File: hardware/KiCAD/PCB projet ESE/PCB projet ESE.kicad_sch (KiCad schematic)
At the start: 49 parts, among them J1 Conn_01x06, J2 Conn_01x04, J3 Conn_01x06, J4 Conn_01x06, J5 Conn_01x02, J6 Conn_01x04, J7 Conn_ST_STDC14, SW1 SW_SPST, SW2 472121010111, U1 ZXBM5210-SP, U2 ZXBM5210-SP, U3 STM32G474RETx, U4 ADXL343

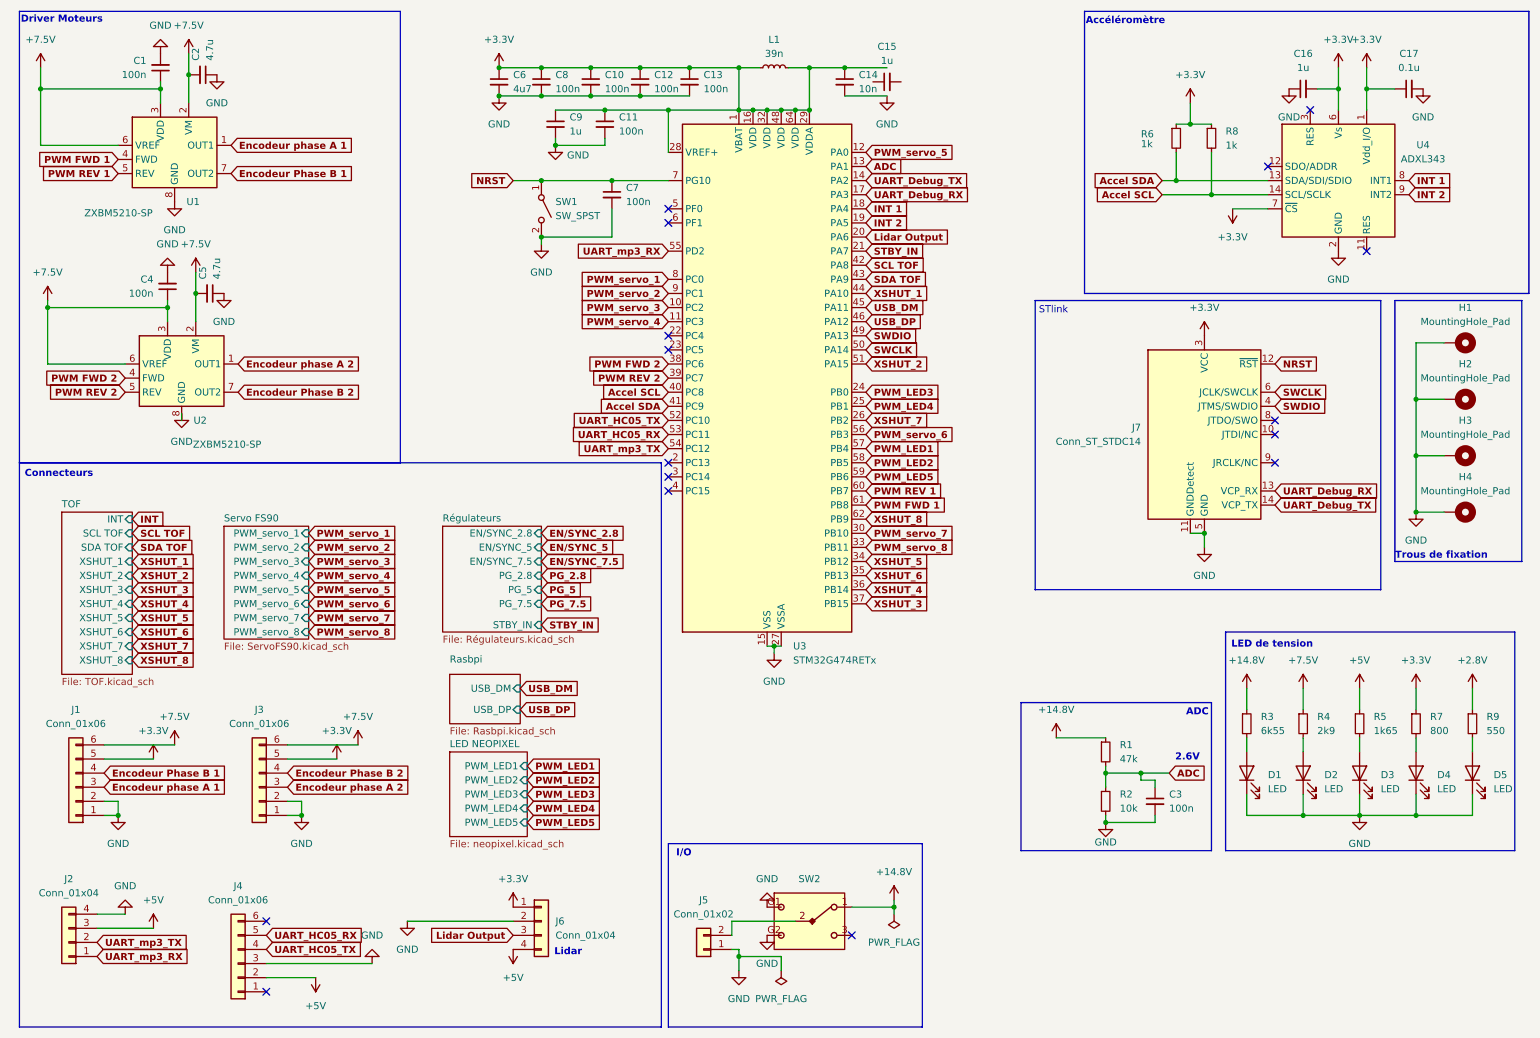
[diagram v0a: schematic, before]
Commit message: maj schematic & pinout CubeIDE
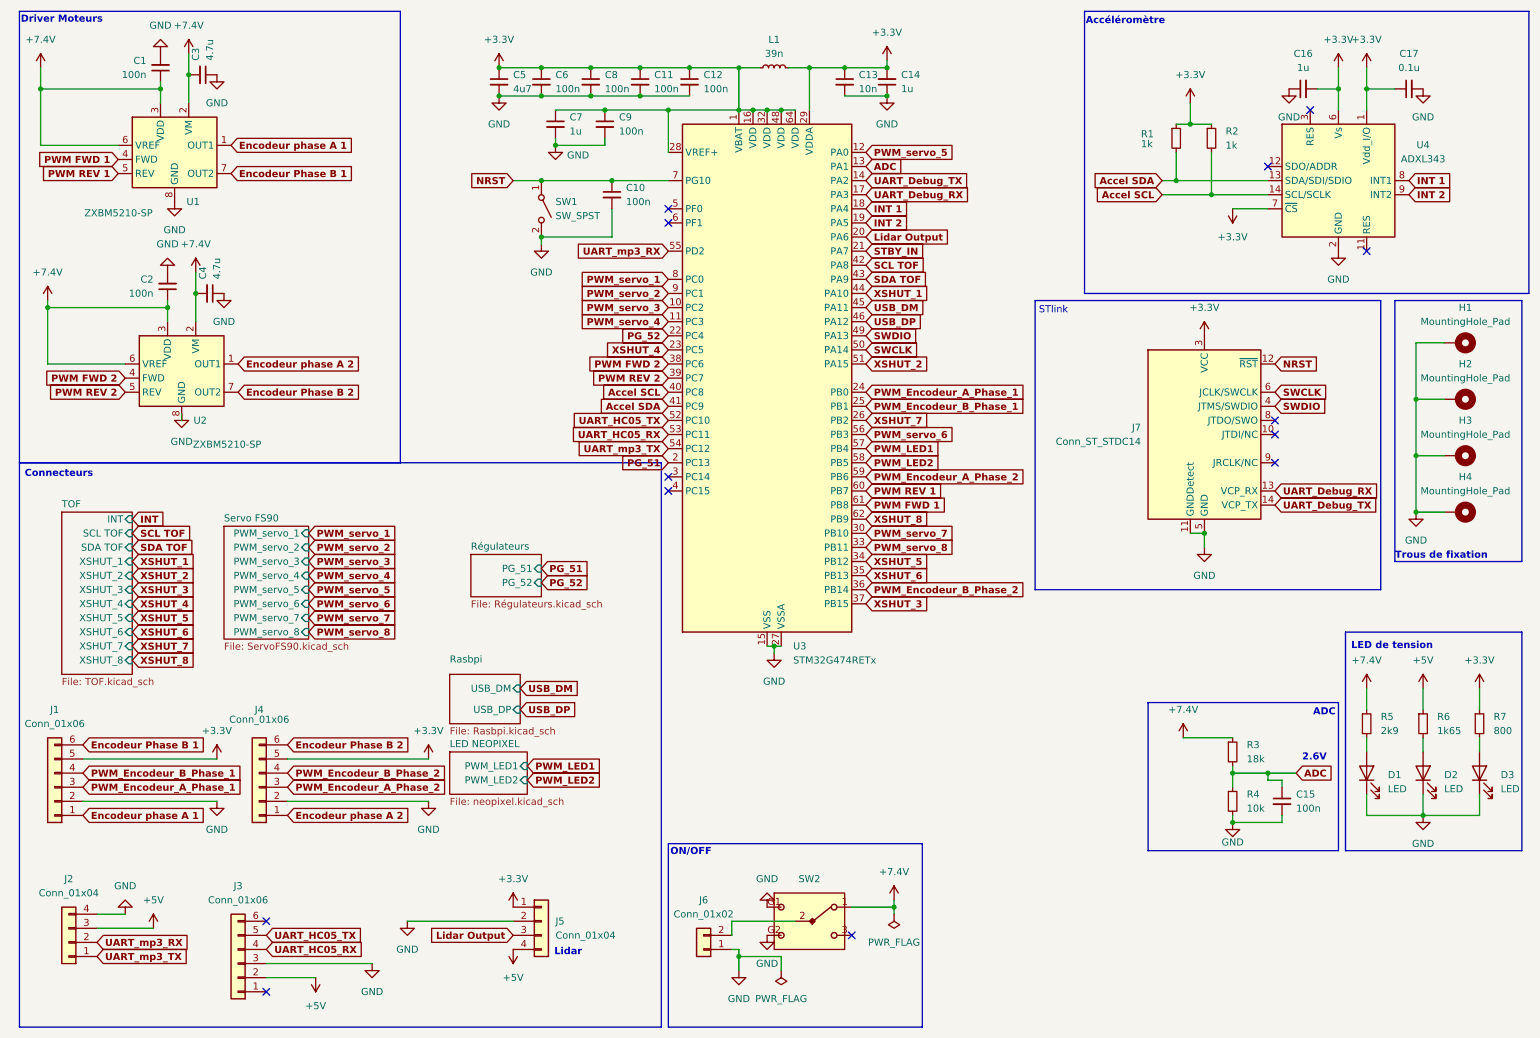
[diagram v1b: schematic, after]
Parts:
- removed D1, D5: LED, LED_SMD:LED_0603_1608Metric, symbol Device:LED
- removed R3: 6k55, Resistor_SMD:R_0402_1005Metric, symbol Device:R_Small
- removed R9: 550, Resistor_SMD:R_0402_1005Metric, symbol Device:R_Small
- J6: renamed from J5; footprint Connector_AMASS:AMASS_XT60-M_1x02_P7.20mm_Vertical -> Connector_AMASS:AMASS_XT30U-M_1x02_P5.0mm_Vertical
- R3: renamed from R1; value 47k -> 18k
- renumbered C7 to C10, C12 to C11, C13 to C12, C14 to C13, C15 to C14, C3 to C15, C4 to C2, C2 to C3, C5 to C4, C6 to C5, C8 to C6, C9 to C7, C10 to C8, C11 to C9, D2 to D1, D3 to D2, D4 to D3, J4 to J3, J3 to J4, J6 to J5, R6 to R1, R8 to R2, R2 to R4, R4 to R5, R5 to R6
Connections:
- net +3.3V: now also C14.2
- net Encodeur Phase B 1: now also J1.6 (Pin_6); no longer J1.4 (Pin_4)
- net Encodeur Phase B 2: now also J4.6 (Pin_6); no longer J4.4 (Pin_4)
- net Encodeur phase A 1: now also J1.1 (Pin_1); no longer J1.3 (Pin_3)
- net Encodeur phase A 2: now also J4.1 (Pin_1); no longer J4.3 (Pin_3)
- net GND: now also C14.1; no longer J1.1 (Pin_1), J4.1 (Pin_1)
- net UART_HC05_RX: now also J3.4 (Pin_4); no longer J3.5 (Pin_5)
- net UART_HC05_TX: now also J3.5 (Pin_5); no longer J3.4 (Pin_4)
- net UART_mp3_RX: now also J2.2 (Pin_2); no longer J2.1 (Pin_1)
- net UART_mp3_TX: now also J2.1 (Pin_1); no longer J2.2 (Pin_2)
- net XSHUT_4: now also U3.23 (PC5); no longer U3.36 (PB14)
- net PG_51: now reaches U3.2 (PC13)
- net PG_52: now reaches U3.22 (PC4)
- net +14.8V renamed +7.4V
- net +7.4V: now also C1.1, C2.1, C3.2, C4.2, R5.1, U1.2 (VM), U1.3 (VDD), U1.6 (VREF), U2.2 (VM), U2.3 (VDD), U2.6 (VREF)
- removed net +7.5V: C1.1, C2.1, C3.2, C4.2, J1.6 (Pin_6), J4.6 (Pin_6), R5.1, U1.2 (VM), U1.3 (VDD), U1.6 (VREF), U2.2 (VM), U2.3 (VDD), U2.6 (VREF)
- net PWM_LED3 renamed PWM_Encodeur_A_Phase_1
- net PWM_Encodeur_A_Phase_1: now also J1.3 (Pin_3)
- net PWM_LED4 renamed PWM_Encodeur_B_Phase_1
- net PWM_Encodeur_B_Phase_1: now also J1.4 (Pin_4)
- net PWM_LED5 renamed PWM_Encodeur_A_Phase_2
- net PWM_Encodeur_A_Phase_2: now also J4.3 (Pin_3)
- new net PWM_Encodeur_B_Phase_2: J4.4 (Pin_4), U3.36 (PB14)
- no-connect marks 16 -> 13
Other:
- sheet LED NEOPIXEL ports: added none; removed PWM_LED3, PWM_LED4, PWM_LED5
- sheet Régulateurs ports: added PG_51, PG_52; removed EN/SYNC_2.8, EN/SYNC_5, EN/SYNC_7.5, PG_2.8, PG_5, PG_7.5, STBY_IN
- note added: "ON/OFF"
- note removed: "I/O"
- moved on the sheet: C14, C15, D1, D2, D3, J1, R3, R4, R5, R6, R7

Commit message: maj schematic
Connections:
- net ADC renamed ADC1_IN2
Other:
- moved on the sheet: C15, R3, R4
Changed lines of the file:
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@@
 	)
 	(rectangle
-		(start 215.9 137.16)
+		(start 210.82 137.16)
 		(end 250.19 163.83)
 		(stroke
@@
 	(text "ADC"
 		(exclude_from_sim no)
-		(at 247.65 138.938 0)
+		(at 242.57 138.938 0)
 		(effects
 			(font
@@
 	(text "2.6V"
 		(exclude_from_sim no)
-		(at 245.872 147.066 0)
+		(at 240.792 147.066 0)
 		(effects
 			(font
@@
 	)
 	(junction
-		(at 231.14 149.86)
+		(at 226.06 149.86)
 		(diameter 0)
 		(color 0 0 0 0)
@@
 	)
 	(junction
-		(at 237.49 149.86)
+		(at 232.41 149.86)
 		(diameter 0)
 		(color 0 0 0 0)
@@
 	)
 	(junction
-		(at 231.14 158.75)
+		(at 226.06 158.75)
 		(diameter 0)
 		(color 0 0 0 0)
@@
 	(wire
 		(pts
-			(xy 231.14 149.86) (xy 231.14 152.4)
+			(xy 226.06 149.86) (xy 226.06 152.4)
 		)
 		(stroke
@@
 	(wire
 		(pts
-			(xy 231.14 148.59) (xy 231.14 149.86)
+			(xy 226.06 148.59) (xy 226.06 149.86)
 		)
 		(stroke
@@
 	(wire
 		(pts
-			(xy 240.03 157.48) (xy 240.03 158.75)
+			(xy 234.95 157.48) (xy 234.95 158.75)
 		)
 		(stroke
@@
 	(wire
 		(pts
-			(xy 231.14 158.75) (xy 231.14 157.48)
+			(xy 226.06 158.75) (xy 226.06 157.48)
 		)
 		(stroke
@@
 	(wire
 		(pts
-			(xy 240.03 158.75) (xy 231.14 158.75)
+			(xy 234.95 158.75) (xy 226.06 158.75)
 		)
 		(stroke
@@
 	(wire
 		(pts
-			(xy 240.03 152.4) (xy 240.03 151.13)
+			(xy 234.95 152.4) (xy 234.95 151.13)
 		)
 		(stroke
@@
 	(wire
 		(pts
-			(xy 237.49 149.86) (xy 231.14 149.86)
+			(xy 232.41 149.86) (xy 226.06 149.86)
 		)
 		(stroke
@@
 	(wire
 		(pts
-			(xy 242.57 149.86) (xy 237.49 149.86)
+			(xy 237.49 149.86) (xy 232.41 149.86)
 		)
 		(stroke
@@
 	(wire
 		(pts
-			(xy 222.25 143.51) (xy 231.14 143.51)
+			(xy 217.17 143.51) (xy 226.06 143.51)
 		)
 		(stroke
@@
 	(wire
 		(pts
-			(xy 237.49 151.13) (xy 237.49 149.86)
+			(xy 232.41 151.13) (xy 232.41 149.86)
 		)
 		(stroke
@@
 	(wire
 		(pts
-			(xy 240.03 151.13) (xy 237.49 151.13)
+			(xy 234.95 151.13) (xy 232.41 151.13)
 		)
 		(stroke
@@
 		)
 	)
-	(global_label "ADC"
+	(global_label "ADC1_IN2"
 		(shape input)
-		(at 242.57 149.86 0)
+		(at 237.49 149.86 0)
 		(fields_autoplaced yes)
 		(effects
@@
 		)
 		(property "Intersheetrefs" "${INTERSHEET_REFS}"
-			(at 249.6598 149.86 0)
+			(at 249.9017 149.86 0)
 			(effects
 				(font
@@
 		)
 	)
-	(global_label "ADC"
+	(global_label "ADC1_IN2"
 		(shape input)
 		(at 165.1 40.64 0)
@@
 		)
 		(property "Intersheetrefs" "${INTERSHEET_REFS}"
-			(at 172.1898 40.64 0)
+			(at 177.5117 40.64 0)
 			(effects
 				(font
@@
 	(symbol
 		(lib_id "Device:R_Small")
-		(at 231.14 154.94 0)
+		(at 226.06 154.94 0)
 		(unit 1)
 		(exclude_from_sim no)
@@
 		(fields_autoplaced yes)
 		(property "Reference" "R4"
-			(at 233.68 153.6699 0)
+			(at 228.6 153.6699 0)
 			(effects
 				(font
@@
 		)
 		(property "Value" "10k"
-			(at 233.68 156.2099 0)
+			(at 228.6 156.2099 0)
 			(effects
 				(font
@@
 		)
 		(property "Footprint" "Resistor_SMD:R_0402_1005Metric"
-			(at 231.14 154.94 0)
+			(at 226.06 154.94 0)
 			(effects
 				(font
@@
 		)
 		(property "Datasheet" "~"
-			(at 231.14 154.94 0)
+			(at 226.06 154.94 0)
 			(effects
 				(font
@@
 		)
 		(property "Description" "Resistor, small symbol"
-			(at 231.14 154.94 0)
+			(at 226.06 154.94 0)
 			(effects
 				(font
@@
 	(symbol
 		(lib_id "Device:R_Small")
-		(at 231.14 146.05 0)
+		(at 226.06 146.05 0)
 		(unit 1)
 		(exclude_from_sim no)
@@
 		(fields_autoplaced yes)
 		(property "Reference" "R3"
-			(at 233.68 144.7799 0)
+			(at 228.6 144.7799 0)
 			(effects
 				(font
@@
 		)
 		(property "Value" "18k"
-			(at 233.68 147.3199 0)
+			(at 228.6 147.3199 0)
 			(effects
 				(font
@@
 		)
 		(property "Footprint" "Resistor_SMD:R_0402_1005Metric"
-			(at 231.14 146.05 0)
+			(at 226.06 146.05 0)
 			(effects
 				(font
@@
 		)
 		(property "Datasheet" "~"
-			(at 231.14 146.05 0)
+			(at 226.06 146.05 0)
 			(effects
 				(font
@@
 		)
 		(property "Description" "Resistor, small symbol"
-			(at 231.14 146.05 0)
+			(at 226.06 146.05 0)
 			(effects
 				(font
@@
 	(symbol
 		(lib_id "power:GND")
-		(at 231.14 158.75 0)
+		(at 226.06 158.75 0)
 		(unit 1)
 		(exclude_from_sim no)
@@
 		(dnp no)
 		(property "Reference" "#PWR037"
-			(at 231.14 165.1 0)
+			(at 226.06 165.1 0)
 			(effects
 				(font
@@
 		)
 		(property "Value" "GND"
-			(at 231.14 162.306 0)
+			(at 226.06 162.306 0)
 			(effects
 				(font
@@
 		)
 		(property "Footprint" ""
-			(at 231.14 158.75 0)
+			(at 226.06 158.75 0)
 			(effects
 				(font
@@
 		)
 		(property "Datasheet" ""
-			(at 231.14 158.75 0)
+			(at 226.06 158.75 0)
 			(effects
 				(font
@@
 		)
 		(property "Description" "Power symbol creates a global label with name \"GND\" , ground"
-			(at 231.14 158.75 0)
+			(at 226.06 158.75 0)
 			(effects
 				(font
@@
 	(symbol
 		(lib_id "power:+7.5V")
-		(at 222.25 143.51 0)
+		(at 217.17 143.51 0)
 		(unit 1)
 		(exclude_from_sim no)
@@
 		(fields_autoplaced yes)
 		(property "Reference" "#PWR032"
-			(at 222.25 147.32 0)
+			(at 217.17 147.32 0)
 			(effects
 				(font
@@
 		)
 		(property "Value" "+7.4V"
-			(at 222.25 138.43 0)
+			(at 217.17 138.43 0)
 			(effects
 				(font
@@
 		)
 		(property "Footprint" ""
-			(at 222.25 143.51 0)
+			(at 217.17 143.51 0)
 			(effects
 				(font
@@
 		)
 		(property "Datasheet" ""
-			(at 222.25 143.51 0)
+			(at 217.17 143.51 0)
 			(effects
 				(font
@@
 		)
 		(property "Description" "Power symbol creates a global label with name \"+7.5V\""
-			(at 222.25 143.51 0)
+			(at 217.17 143.51 0)
 			(effects
 				(font
@@
 	(symbol
 		(lib_id "Device:C_Small")
-		(at 240.03 154.94 0)
+		(at 234.95 154.94 0)
 		(unit 1)
 		(exclude_from_sim no)
@@
 		(fields_autoplaced yes)
 		(property "Reference" "C15"
-			(at 242.57 153.6762 0)
+			(at 237.49 153.6762 0)
 			(effects
 				(font
@@
 		)
 		(property "Value" "100n"
-			(at 242.57 156.2162 0)
+			(at 237.49 156.2162 0)
 			(effects
 				(font
@@
 		)
 		(property "Footprint" "Capacitor_SMD:C_0402_1005Metric"
-			(at 240.03 154.94 0)
+			(at 234.95 154.94 0)
 			(effects
 				(font
@@
 		)
 		(property "Datasheet" "~"
-			(at 240.03 154.94 0)
+			(at 234.95 154.94 0)
 			(effects
 				(font
@@
 		)
 		(property "Description" "Unpolarized capacitor, small symbol"
-			(at 240.03 154.94 0)
+			(at 234.95 154.94 0)
 			(effects
 				(font

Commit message: maj schematic
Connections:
- net PWM_servo_1: no longer names the net of U3.8 (PC0)
- net PWM_servo_2: no longer names the net of U3.9 (PC1)
- net PWM_servo_3: no longer names the net of U3.10 (PC2)
- net PWM_servo_4: no longer names the net of U3.11 (PC3)
- net PWM_servo_5: no longer names the net of U3.12 (PA0)
- net PWM_servo_6: no longer names the net of U3.56 (PB3)
- net PWM_servo_7: no longer names the net of U3.30 (PB10)
- net PWM_servo_8: no longer names the net of U3.33 (PB11)
- net STBY_IN: no longer names the net of U3.21 (PA7)
- no-connect marks 13 -> 22
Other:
- removed sheet Servo FS90

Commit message: maj schematic et pinout
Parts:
- added J16: Conn_01x03, Connector_JST:JST_PH_B3B-PH-K_1x03_P2.00mm_Vertical, symbol Connector_Generic:Conn_01x03
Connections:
- net +5V: now also J16.3 (Pin_3)
- net GND: now also J16.1 (Pin_1)
- net PWM FWD 2: now also U3.59 (PB6); no longer U3.38 (PC6)
- net PWM REV 2: now also U3.62 (PB9); no longer U3.39 (PC7)
- net PWM_LED1: now also J16.2 (Pin_2)
- net XSHUT_8: now also U3.21 (PA7); no longer U3.62 (PB9)
- net Encodeur_B_Phase_1: now reaches U3.8 (PC0)
- net Encodeur_B_Phase_1: now also J1.4 (Pin_4)
- net Encodeur_A_Phase_1: now reaches U3.9 (PC1)
- net Encodeur_A_Phase_1: now also J1.3 (Pin_3)
- net Encodeur Phase B 1 renamed Moteur + 1
- net Moteur + 1: now also U1.1 (OUT1); no longer U1.7 (OUT2)
- net Encodeur Phase B 2 renamed Moteur + 2
- net Moteur + 2: now also U2.1 (OUT1); no longer U2.7 (OUT2)
- net Encodeur phase A 1 renamed Moteur - 1
- net Moteur - 1: now also U1.7 (OUT2); no longer U1.1 (OUT1)
- net Encodeur phase A 2 renamed Moteur - 2
- net Moteur - 2: now also U2.7 (OUT2); no longer U2.1 (OUT1)
- net PWM_Encodeur_A_Phase_1: no longer names the net of U3.24 (PB0)
- net PWM_Encodeur_A_Phase_1: no longer J1.3 (Pin_3)
- net PWM_Encodeur_A_Phase_2 renamed Encodeur_A_Phase_2
- net Encodeur_A_Phase_2: now also U3.38 (PC6); no longer U3.59 (PB6)
- net PWM_Encodeur_B_Phase_1: no longer names the net of U3.25 (PB1)
- net PWM_Encodeur_B_Phase_1: no longer J1.4 (Pin_4)
- net PWM_Encodeur_B_Phase_2: no longer names the net of U3.36 (PB14)
- net PWM_Encodeur_B_Phase_2: no longer J4.4 (Pin_4)
- net PWM_LED2: no longer names the net of U3.58 (PB5)
- new net Encodeur_B_Phase_2: J4.4 (Pin_4), U3.39 (PC7)
- no-connect marks 22 -> 23
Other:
- removed sheet LED NEOPIXEL
- note added: "Neopixel"

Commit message: update pcb
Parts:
- J2: footprint Connector_JST:JST_PH_B4B-PH-K_1x04_P2.00mm_Vertical -> Connector_JST:JST_SH_BM04B-SRSS-TB_1x04-1MP_P1.00mm_Vertical
- J3: footprint Connector_JST:JST_PH_B6B-PH-K_1x06_P2.00mm_Vertical -> Connector_JST:JST_SH_BM06B-SRSS-TB_1x06-1MP_P1.00mm_Vertical
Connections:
- net INT_8: now reaches U3.12 (PA0)
- net INT_4: now reaches U3.24 (PB0)
- net INT_3: now reaches U3.25 (PB1)
- net INT_6: now reaches U3.30 (PB10)
- net INT_5: now reaches U3.33 (PB11)
- net INT_7: now reaches U3.36 (PB14)
- net INT_2: now reaches U3.56 (PB3)
- net INT_1: now reaches U3.58 (PB5)
- no-connect marks 23 -> 15
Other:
- sheet TOF ports: added INT 1, INT 2, INT 3, INT 4, INT 5, INT 6, INT 7, INT 8; removed INT
